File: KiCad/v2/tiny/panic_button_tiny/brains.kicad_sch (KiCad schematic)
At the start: 24 parts, among them J3 PINHD_1x6_Male, SW1 Switch_Tactile_CnK, SW2 Switch_Tactile_CnK, SW3 Switch_Tactile_CnK, U5 ESP32-C3, Y1 C3E40000121010X, Y2 CTS3-32.768-12.5-20-R

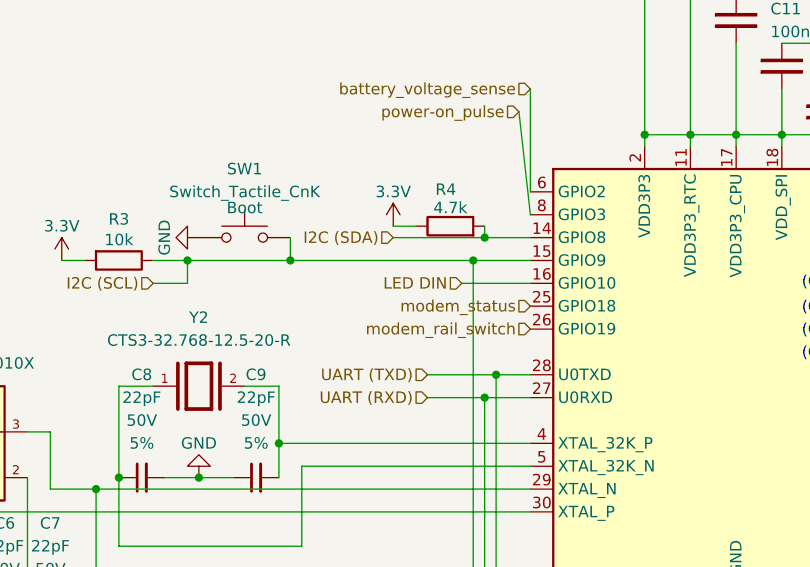
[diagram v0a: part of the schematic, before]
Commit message: [UPDATE] connections in the circuit schematic
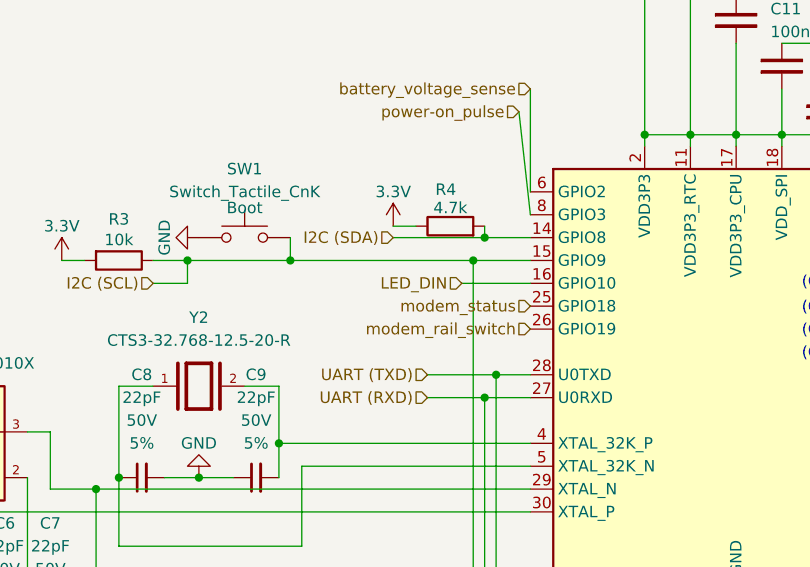
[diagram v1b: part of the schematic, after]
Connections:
- net LED DIN renamed LED_DIN
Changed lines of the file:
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@@
 		)
 	)
-	(hierarchical_label "LED DIN"
+	(hierarchical_label "LED_DIN"
 		(shape input)
 		(at 78.74 57.15 180)

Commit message: [UPDATE] the schematic wirering
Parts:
- removed C6, C7, C8, C9: 22pF, PCM_SparkFun-Capacitor:C_0402_1005Metric, symbol PCM_SparkFun-Capacitor:22pF_0402_50V_5%
- removed J3: PINHD_1x6_Male, Connector_PinHeader_2.54mm:PinHeader_1x06_P2.54mm_Vertical, symbol PCM_SL_Pin_Headers:PINHD_1x6_Male
- removed TP1: 3.3V, TestPoint:TestPoint_Pad_D4.0mm, symbol Connector:TestPoint
- removed TP2: U0TXD, TestPoint:TestPoint_Pad_D4.0mm, symbol Connector:TestPoint
- removed TP3: CHIP_EN, TestPoint:TestPoint_Pad_D4.0mm, symbol Connector:TestPoint
- removed TP4: GND, TestPoint:TestPoint_Pad_D4.0mm, symbol Connector:TestPoint
- removed TP5: U0RXD, TestPoint:TestPoint_Pad_D4.0mm, symbol Connector:TestPoint
- removed TP6: GPIO9, TestPoint:TestPoint_Pad_D4.0mm, symbol Connector:TestPoint
- removed Y1: C3E40000121010X, C3E40000121010X:XTAL_C3E40000121010X, symbol C3E40000121010X:C3E40000121010X
- removed Y2: CTS3-32.768-12.5-20-R, CTS3-32.768-12.5-20-R:XTAL_CTS3-32.768-12.5-20-R, symbol CTS3-32.768-12.5-20-R:CTS3-32.768-12.5-20-R
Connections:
- net Clock/XTAL_N: now reaches U5.29 (XTAL_N)
- net Clock/XTAL_P: now reaches U5.30 (XTAL_P)
- net UART/UART_CHIP_EN: now reaches R5.1, SW2.1, U5.7 (CHIP_EN)
- net Clock/XTAL_32K_P: now reaches U5.5 (XTAL_32K_N)
- net Clock/XTAL_32K_N: now reaches U5.4 (XTAL_32K_P)
- net Buzzer+: now reaches U5.13 (MTDO)
- no-connect marks 0 -> 1
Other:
- added sheet Clock (clock.kicad_sch)
- added sheet UART (uart.kicad_sch)

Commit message: [UPDATE] the schematics annotations
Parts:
- renumbered C10 to C6, C11 to C7, C12 to C8, C13 to C9

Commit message: [UPDATE] connections in the schematic to better represent the logic flow
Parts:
- renumbered C8 to C10, C9 to C11, C6 to C8, C7 to C9
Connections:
- net Clock/XTAL_32K_N: now also U5.5 (XTAL_32K_N); no longer U5.4 (XTAL_32K_P)
- net Clock/XTAL_32K_P: now also U5.4 (XTAL_32K_P); no longer U5.5 (XTAL_32K_N)
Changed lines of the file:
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@@
+	(wire
+		(pts
+			(xy 76.2 77.47) (xy 86.36 77.47)
+		)
+		(stroke
+			(width 0)
+			(type default)
+		)
+	)
+	(wire
+		(pts
+			(xy 76.2 74.93) (xy 86.36 74.93)
+		)
+		(stroke
+			(width 0)
+			(type default)
+		)
+	)
 	(wire
 		(pts
@@
 	(wire
 		(pts
-			(xy 76.2 74.93) (xy 86.36 74.93)
-		)
-		(stroke
-			(width 0)
-			(type default)
-		)
-	)
-	(wire
-		(pts
 			(xy 135.89 59.69) (xy 132.08 59.69)
 		)
@@
 		(pts
 			(xy 76.2 82.55) (xy 86.36 82.55)
-		)
-		(stroke
-			(width 0)
-			(type default)
-		)
-	)
-	(wire
-		(pts
-			(xy 76.2 77.47) (xy 86.36 77.47)
 		)
 		(stroke
@@
 		(dnp no)
 		(fields_autoplaced yes)
-		(property "Reference" "#PWR058"
+		(property "Reference" "#PWR061"
 			(at 166.37 53.34 0)
 			(hide yes)
@@
 			(project "panic_button_tiny"
 				(path "/c4eb92e9-b42f-4db0-b1d9-0ef70f7ca601/525ab16f-d6f3-4728-a011-f4f1ced9fd5e"
-					(reference "#PWR058")
+					(reference "#PWR061")
 					(unit 1)
 				)
@@
 		(dnp no)
 		(fields_autoplaced yes)
-		(property "Reference" "C9"
+		(property "Reference" "C11"
 			(at 123.19 36.8299 90)
 			(show_name no)
@@
 			(project "panic_button_tiny"
 				(path "/c4eb92e9-b42f-4db0-b1d9-0ef70f7ca601/525ab16f-d6f3-4728-a011-f4f1ced9fd5e"
-					(reference "C9")
+					(reference "C11")
 					(unit 1)
 				)
@@
 		(dnp no)
 		(fields_autoplaced yes)
-		(property "Reference" "#PWR055"
+		(property "Reference" "#PWR058"
 			(at 99.06 21.59 0)
 			(hide yes)
@@
 			(project "panic_button_tiny"
 				(path "/c4eb92e9-b42f-4db0-b1d9-0ef70f7ca601/525ab16f-d6f3-4728-a011-f4f1ced9fd5e"
-					(reference "#PWR055")
+					(reference "#PWR058")
 					(unit 1)
 				)
@@
 		(dnp no)
 		(fields_autoplaced yes)
-		(property "Reference" "#PWR054"
+		(property "Reference" "#PWR057"
 			(at 71.12 54.61 0)
 			(hide yes)
@@
 			(project "panic_button_tiny"
 				(path "/c4eb92e9-b42f-4db0-b1d9-0ef70f7ca601/525ab16f-d6f3-4728-a011-f4f1ced9fd5e"
-					(reference "#PWR054")
+					(reference "#PWR057")
 					(unit 1)
 				)
@@
 		(dnp no)
 		(fields_autoplaced yes)
-		(property "Reference" "C6"
+		(property "Reference" "C8"
 			(at 107.95 19.0499 90)
 			(show_name no)
@@
 			(project "panic_button_tiny"
 				(path "/c4eb92e9-b42f-4db0-b1d9-0ef70f7ca601/525ab16f-d6f3-4728-a011-f4f1ced9fd5e"
-					(reference "C6")
+					(reference "C8")
 					(unit 1)
 				)
@@
 		(dnp no)
 		(fields_autoplaced yes)
-		(property "Reference" "#PWR057"
+		(property "Reference" "#PWR060"
 			(at 140.97 41.91 0)
 			(hide yes)
@@
 			(project "panic_button_tiny"
 				(path "/c4eb92e9-b42f-4db0-b1d9-0ef70f7ca601/525ab16f-d6f3-4728-a011-f4f1ced9fd5e"
-					(reference "#PWR057")
+					(reference "#PWR060")
 					(unit 1)
 				)
@@
 		(dnp no)
 		(fields_autoplaced yes)
-		(property "Reference" "#PWR052"
+		(property "Reference" "#PWR055"
 			(at 34.29 58.42 0)
 			(hide yes)
@@
 			(project "panic_button_tiny"
 				(path "/c4eb92e9-b42f-4db0-b1d9-0ef70f7ca601/525ab16f-d6f3-4728-a011-f4f1ced9fd5e"
-					(reference "#PWR052")
+					(reference "#PWR055")
 					(unit 1)
 				)
@@
 		(dnp no)
 		(fields_autoplaced yes)
-		(property "Reference" "#PWR060"
+		(property "Reference" "#PWR063"
 			(at 199.39 63.5 0)
 			(hide yes)
@@
 			(project "panic_button_tiny"
 				(path "/c4eb92e9-b42f-4db0-b1d9-0ef70f7ca601/525ab16f-d6f3-4728-a011-f4f1ced9fd5e"
-					(reference "#PWR060")
+					(reference "#PWR063")
 					(unit 1)
 				)
@@
 		(dnp no)
 		(fields_autoplaced yes)
-		(property "Reference" "C7"
+		(property "Reference" "C9"
 			(at 113.03 26.6699 90)
 			(show_name no)
@@
 			(project "panic_button_tiny"
 				(path "/c4eb92e9-b42f-4db0-b1d9-0ef70f7ca601/525ab16f-d6f3-4728-a011-f4f1ced9fd5e"
-					(reference "C7")
+					(reference "C9")
 					(unit 1)
 				)
@@
 		(dnp no)
 		(fields_autoplaced yes)
-		(property "Reference" "#PWR059"
+		(property "Reference" "#PWR062"
 			(at 180.34 55.88 0)
 			(hide yes)
@@
 			(project "panic_button_tiny"
 				(path "/c4eb92e9-b42f-4db0-b1d9-0ef70f7ca601/525ab16f-d6f3-4728-a011-f4f1ced9fd5e"
-					(reference "#PWR059")
+					(reference "#PWR062")
 					(unit 1)
 				)
@@
 		(dnp no)
 		(fields_autoplaced yes)
-		(property "Reference" "#PWR056"
+		(property "Reference" "#PWR059"
 			(at 109.22 102.87 0)
 			(hide yes)
@@
 			(project "panic_button_tiny"
 				(path "/c4eb92e9-b42f-4db0-b1d9-0ef70f7ca601/525ab16f-d6f3-4728-a011-f4f1ced9fd5e"
-					(reference "#PWR056")
+					(reference "#PWR059")
 					(unit 1)
 				)
@@
 		(dnp no)
 		(fields_autoplaced yes)
-		(property "Reference" "C8"
+		(property "Reference" "C10"
 			(at 118.11 31.7499 90)
 			(show_name no)
@@
 			(project "panic_button_tiny"
 				(path "/c4eb92e9-b42f-4db0-b1d9-0ef70f7ca601/525ab16f-d6f3-4728-a011-f4f1ced9fd5e"
-					(reference "C8")
+					(reference "C10")
 					(unit 1)
 				)
@@
 		(dnp no)
 		(fields_autoplaced yes)
-		(property "Reference" "#PWR053"
+		(property "Reference" "#PWR056"
 			(at 43.18 52.07 0)
 			(hide yes)
@@
 			(project "panic_button_tiny"
 				(path "/c4eb92e9-b42f-4db0-b1d9-0ef70f7ca601/525ab16f-d6f3-4728-a011-f4f1ced9fd5e"
-					(reference "#PWR053")
+					(reference "#PWR056")
 					(unit 1)
 				)
@@
 			)
 		)
-		(pin "UART_GPIO9" output
-			(at 137.16 109.22 180)
-			(effects
-				(font
-					(size 1.27 1.27)
-				)
-				(justify left)
-			)
-		)
-		(pin "UART_U0RXD" output
-			(at 137.16 114.3 180)
-			(effects
-				(font
-					(size 1.27 1.27)
-				)
-				(justify left)
-			)
-		)
 		(pin "UART_U0TXD" output
 			(at 137.16 111.76 180)
+			(effects
+				(font
+					(size 1.27 1.27)
+				)
+				(justify left)
+			)
+		)
+		(pin "UART_U0RXD" output
+			(at 137.16 109.22 180)
+			(effects
+				(font
+					(size 1.27 1.27)
+				)
+				(justify left)
+			)
+		)
+		(pin "UART_GPIO9" output
+			(at 137.16 114.3 180)
 			(effects
 				(font
@@
 		)
 		(pin "XTAL_32K_N" input
+			(at 76.2 77.47 0)
+			(effects
+				(font
+					(size 1.27 1.27)
+				)
+				(justify right)
+			)
+		)
+		(pin "XTAL_32K_P" input
 			(at 76.2 74.93 0)
 			(effects
 				(font
-					(size 1.27 1.27)
-				)
-				(justify right)
-			)
-		)
-		(pin "XTAL_32K_P" input
-			(at 76.2 77.47 0)
-			(effects
-				(font

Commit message: [UPDATE] the schematic with the connections
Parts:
- renumbered R3 to R5, R4 to R6, R5 to R7
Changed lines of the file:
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@@
 		(in_pos_files yes)
 		(dnp no)
-		(property "Reference" "R4"
+		(property "Reference" "R6"
 			(at 76.962 46.736 90)
 			(show_name no)
@@
 			(project "panic_button_tiny"
 				(path "/c4eb92e9-b42f-4db0-b1d9-0ef70f7ca601/525ab16f-d6f3-4728-a011-f4f1ced9fd5e"
-					(reference "R4")
+					(reference "R6")
 					(unit 1)
 				)
@@
 		(in_pos_files yes)
 		(dnp no)
-		(property "Reference" "R3"
+		(property "Reference" "R5"
 			(at 40.64 50.038 90)
 			(show_name no)
@@
 			(project "panic_button_tiny"
 				(path "/c4eb92e9-b42f-4db0-b1d9-0ef70f7ca601/525ab16f-d6f3-4728-a011-f4f1ced9fd5e"
-					(reference "R3")
+					(reference "R5")
 					(unit 1)
 				)
@@
 		(in_pos_files yes)
 		(dnp no)
-		(property "Reference" "R5"
+		(property "Reference" "R7"
 			(at 171.196 49.784 90)
 			(show_name no)
@@
 			(project "panic_button_tiny"
 				(path "/c4eb92e9-b42f-4db0-b1d9-0ef70f7ca601/525ab16f-d6f3-4728-a011-f4f1ced9fd5e"
-					(reference "R5")
-					(unit 1)
-				)
+					(reference "R7")
+					(unit 1)
+				)
